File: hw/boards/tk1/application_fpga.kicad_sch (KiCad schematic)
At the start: 38 parts, among them U10 PT2043AT6, U6 ICE40UP5K-SG48ITR, U8 XT25F08BDFIGT-S

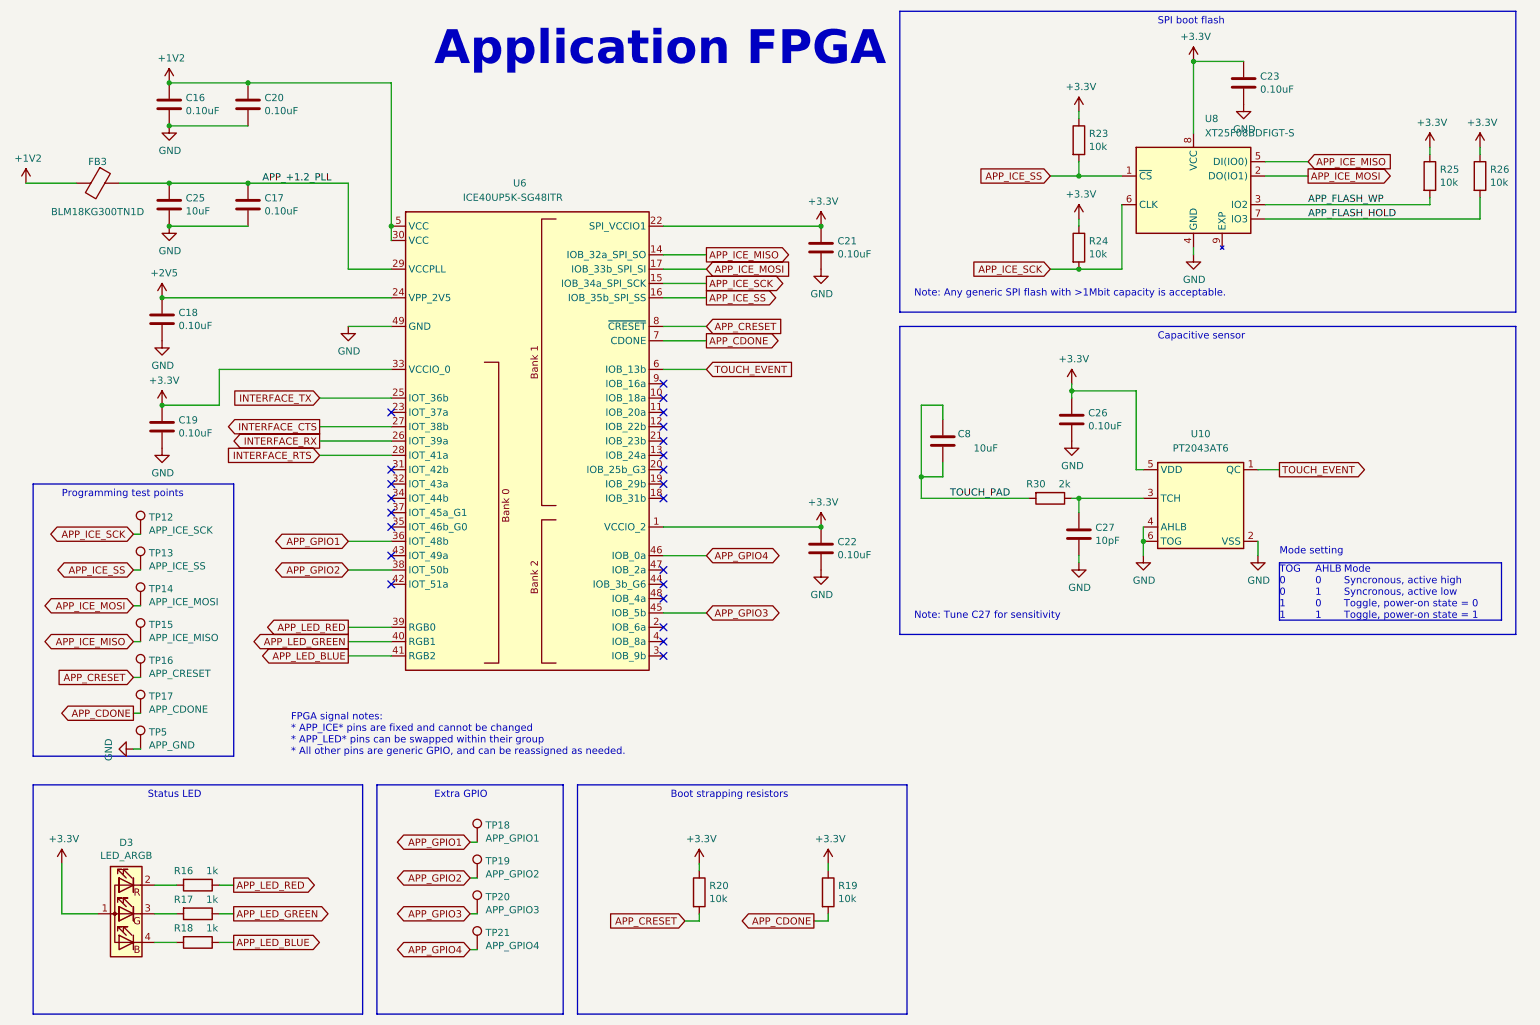
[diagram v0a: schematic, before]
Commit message: Update component values for TK1 PCB
* Use specific part # for C8
* Change flash back to Winbond part, for easier sourcing
* Change C1 to 1pF
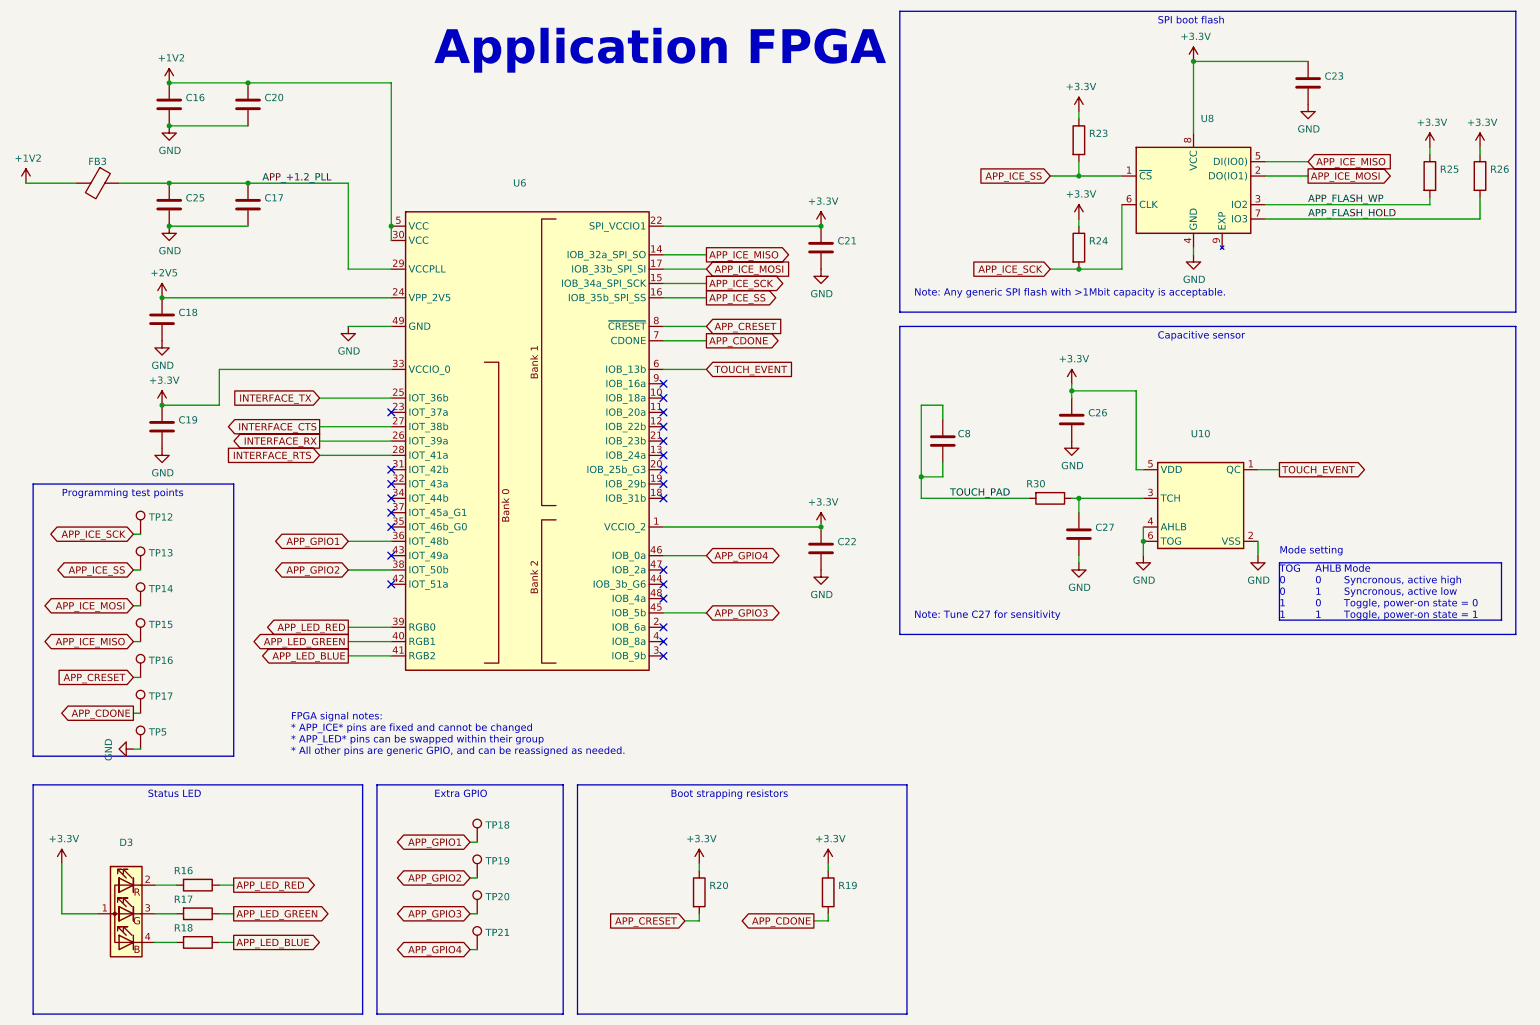
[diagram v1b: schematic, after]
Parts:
- C16, C17, C18, C19, C20, C21, C22, C23, C26: value 0.10uF -> (none); footprint mta1:CAPC1005X06L -> (none)
- C25: value 10uF -> (none); footprint mta1:CAPC1608X09L -> (none)
- C27: value 10pF -> (none); footprint mta1:CAPC1005X06L -> (none)
- C8: value 10uF -> (none); footprint Capacitor_SMD:C_1206_3216Metric -> (none); Extended Value 16V -> 50V,X7R,10%,1.6mm thickness; Manufacturer (none) -> TDK Corporation; Manufacturer Part Number (none) -> C3216X7R1H105K160AE; Supplier (none) -> Digikey; Supplier Part Number (none) -> 445-8904-2-ND
- D3: value LED_ARGB -> (none); footprint mta1:0402rgb-1010 -> (none)
- FB3: value BLM18KG300TN1D -> (none); footprint mta1:Ferritbead_0603_1608Metric -> (none)
- R16, R17, R18: value 1k -> (none); footprint mta1:ERJ2G(0402)_L -> (none)
- R19, R20, R23, R24, R25, R26: value 10k -> (none); footprint mta1:ERJ2G(0402)_L -> (none)
- R30: value 2k -> (none); footprint mta1:ERJ2G(0402)_L -> (none)
- TP12: value APP_ICE_SCK -> (none); footprint TestPoint:TestPoint_Pad_D1.0mm -> (none)
- TP13: value APP_ICE_SS -> (none); footprint TestPoint:TestPoint_Pad_D1.0mm -> (none)
- TP14: value APP_ICE_MOSI -> (none); footprint TestPoint:TestPoint_Pad_D1.0mm -> (none)
- TP15: value APP_ICE_MISO -> (none); footprint TestPoint:TestPoint_Pad_D1.0mm -> (none)
- TP16: value APP_CRESET -> (none); footprint TestPoint:TestPoint_Pad_D1.0mm -> (none)
- TP17: value APP_CDONE -> (none); footprint TestPoint:TestPoint_Pad_D1.0mm -> (none)
- TP18: value APP_GPIO1 -> (none); footprint TestPoint:TestPoint_Pad_D1.0mm -> (none)
- TP19: value APP_GPIO2 -> (none); footprint TestPoint:TestPoint_Pad_D1.0mm -> (none)
- TP20: value APP_GPIO3 -> (none); footprint TestPoint:TestPoint_Pad_D1.0mm -> (none)
- TP21: value APP_GPIO4 -> (none); footprint TestPoint:TestPoint_Pad_D1.0mm -> (none)
- TP5: value APP_GND -> (none); footprint TestPoint:TestPoint_Pad_D1.0mm -> (none)
- U10: value PT2043AT6 -> (none); footprint Package_TO_SOT_SMD:SOT-23-6 -> (none)
- U6: value ICE40UP5K-SG48ITR -> (none); footprint Package_DFN_QFN:QFN-48-1EP_7x7mm_P0.5mm_EP5.6x5.6mm -> (none)
- U8: value XT25F08BDFIGT-S -> (none); footprint mta1:W25Q80DVUXIE -> (none); Manufacturer XTX -> Winbond Electronics; Manufacturer Part Number XT25F08BDFIGT-S -> W25Q80DVUXIE; Supplier LCSC -> Digikey; Supplier Part Number C558860 -> W25Q80DVUXIETR-ND
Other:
- moved on the sheet: C23

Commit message: TK-1 release
* Add dimensions for PCB
* Add layer stackup for PCB
* Change PCB component origin to match expanded board
* Change schematic title to 'TK-1', update release date
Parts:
- C16, C17, C18, C19, C20, C21, C22, C23, C26: value (none) -> 0.10uF; footprint (none) -> mta1:CAPC1005X06L
- C25: value (none) -> 10uF; footprint (none) -> mta1:CAPC1608X09L
- C27: value (none) -> 1pF; footprint (none) -> mta1:CAPC1005X06L
- C8: value (none) -> 1uF; footprint (none) -> Capacitor_SMD:C_1206_3216Metric
- D3: value (none) -> LED_ARGB; footprint (none) -> mta1:0402rgb-1010
- FB3: value (none) -> BLM18KG300TN1D; footprint (none) -> mta1:Ferritbead_0603_1608Metric
- R16, R17, R18: value (none) -> 1k; footprint (none) -> mta1:ERJ2G(0402)_L
- R19, R20, R23, R24, R25, R26: value (none) -> 10k; footprint (none) -> mta1:ERJ2G(0402)_L
- R30: value (none) -> 2k; footprint (none) -> mta1:ERJ2G(0402)_L
- TP12: value (none) -> APP_ICE_SCK; footprint (none) -> mta1:TestPoint_Pad_D1.0mm
- TP13: value (none) -> APP_ICE_SS; footprint (none) -> mta1:TestPoint_Pad_D1.0mm
- TP14: value (none) -> APP_ICE_MOSI; footprint (none) -> mta1:TestPoint_Pad_D1.0mm
- TP15: value (none) -> APP_ICE_MISO; footprint (none) -> mta1:TestPoint_Pad_D1.0mm
- TP16: value (none) -> APP_CRESET; footprint (none) -> mta1:TestPoint_Pad_D1.0mm
- TP17: value (none) -> APP_CDONE; footprint (none) -> mta1:TestPoint_Pad_D1.0mm
- TP18: value (none) -> APP_GPIO1; footprint (none) -> mta1:TestPoint_Pad_D1.0mm
- TP19: value (none) -> APP_GPIO2; footprint (none) -> mta1:TestPoint_Pad_D1.0mm
- TP20: value (none) -> APP_GPIO3; footprint (none) -> mta1:TestPoint_Pad_D1.0mm
- TP21: value (none) -> APP_GPIO4; footprint (none) -> mta1:TestPoint_Pad_D1.0mm
- TP5: value (none) -> APP_GND; footprint (none) -> mta1:TestPoint_Pad_D1.0mm
- U10: value (none) -> PT2043AT6; footprint (none) -> Package_TO_SOT_SMD:SOT-23-6
- U6: value (none) -> ICE40UP5K-SG48ITR; footprint (none) -> Package_DFN_QFN:QFN-48-1EP_7x7mm_P0.5mm_EP5.6x5.6mm
- U8: value (none) -> W25Q80DVUXIE; footprint (none) -> mta1:W25Q80DVUXIE

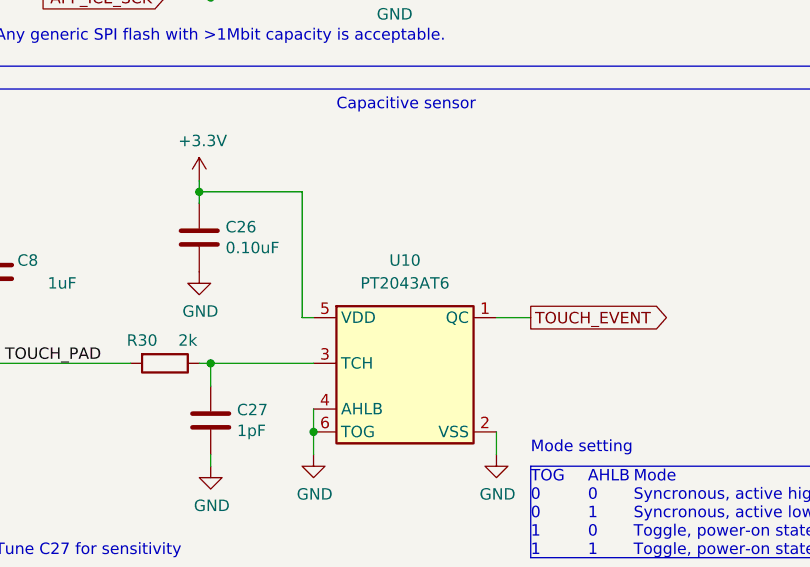
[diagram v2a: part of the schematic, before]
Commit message: TK-1: RevA.1 release
* Add two fiducials to TK-1 board
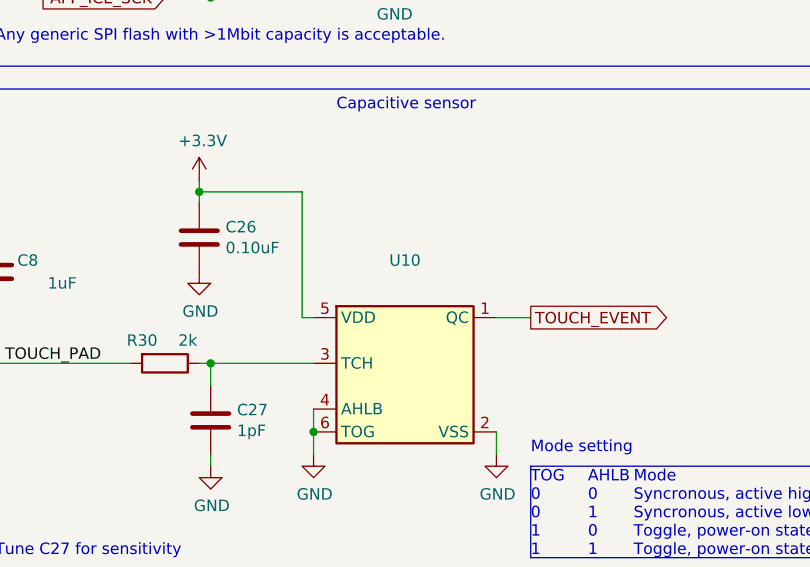
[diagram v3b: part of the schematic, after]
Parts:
- U10: value PT2043AT6 -> (none); footprint Package_TO_SOT_SMD:SOT-23-6 -> (none)
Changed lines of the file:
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@@
     (in_bom yes) (on_board yes) (fields_autoplaced)
     (property "Reference" "U10" (id 0) (at 224.79 90.17 0))
-    (property "Value" "PT2043AT6" (id 1) (at 224.79 92.71 0))
-    (property "Footprint" "Package_TO_SOT_SMD:SOT-23-6" (id 2) (at 203.2 90.17 0)
+    (property "Value" "" (id 1) (at 224.79 92.71 0))
+    (property "Footprint" "" (id 2) (at 203.2 90.17 0)
       (effects (font (size 1.27 1.27)) hide)
     )
